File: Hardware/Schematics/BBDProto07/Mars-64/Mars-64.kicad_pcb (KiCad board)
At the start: 4 copper layers, 50.8 x 50.8 mm, 76 parts, among them J101 Conn_Coaxial, J102 Conn_Coaxial, U101 ADG731, U102 ADG731

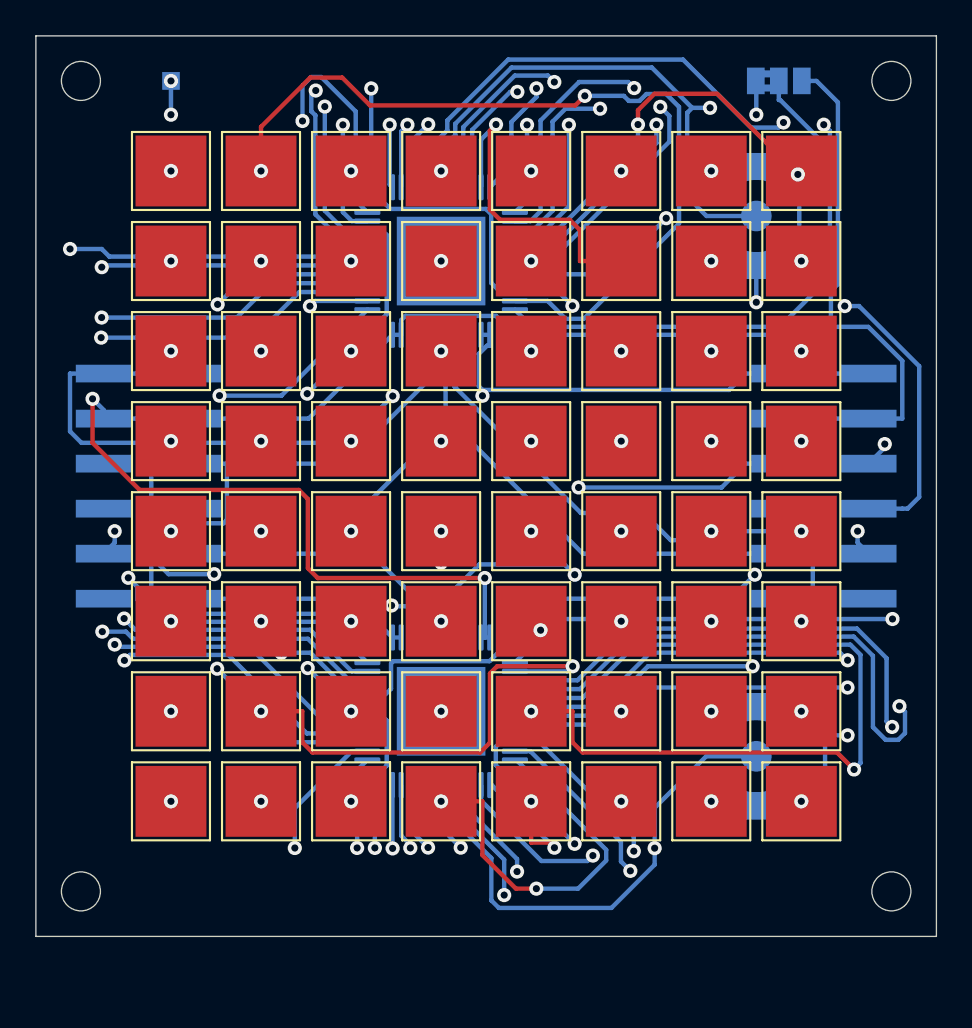
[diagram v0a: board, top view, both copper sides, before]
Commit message: Changed the position of the Pmod pads
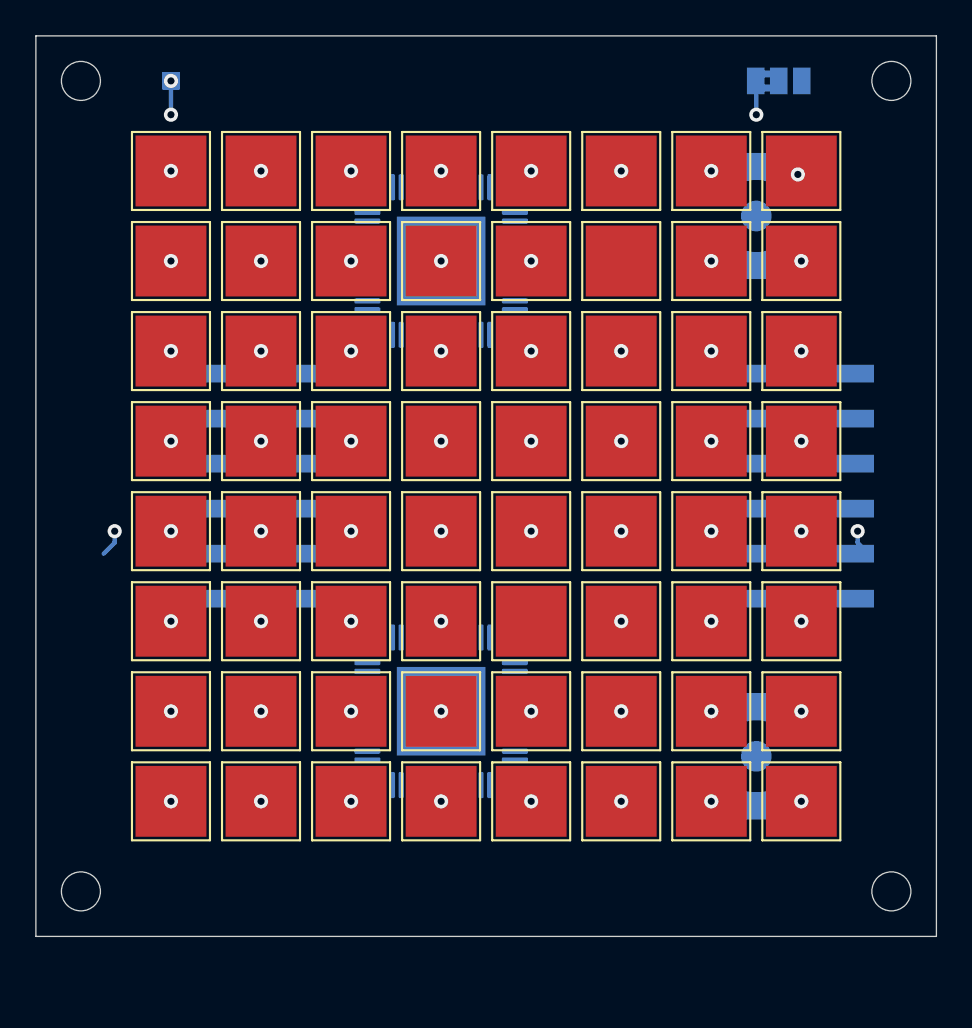
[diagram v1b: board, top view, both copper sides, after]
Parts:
- moved PmodF2 6.35 mm to (48.3, 55.9)
- moved PmodM1 1.27 mm to (78.7, 55.9)
- renumbered Pmod2 to PmodF2, Pmod1 to PmodM1
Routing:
- net GND: track 110.2 -> 0.00 mm, vias 2 -> 0
- net /VCC3V3: track 85.2 -> 0.00 mm, vias 2 -> 0
- net Net-(TP217-Pad1): track 83.9 -> 0.00 mm, vias 2 -> 1
- net Net-(TP208-Pad1): track 82.4 -> 0.00 mm, vias 2 -> 1
- net /SPI_CLK: track 78.6 -> 0.00 mm, vias 3 -> 0
- net Net-(TP123-Pad1): track 70.9 -> 0.00 mm, vias 2 -> 1
- net Net-(TP101-Pad1): track 69.0 -> 0.00 mm, vias 2 -> 1
- net /~SPI_CE: track 64.3 -> 0.00 mm, vias 2 -> 0
- net /DA: track 63.2 -> 0.00 mm, vias 2 -> 0
- net Net-(TP119-Pad1): track 62.1 -> 0.00 mm, vias 2 -> 1
- net /DB: track 61.7 -> 0.00 mm, vias 2 -> 0
- net Net-(TP122-Pad1): track 61.3 -> 0.00 mm, vias 2 -> 1
- net Net-(J101-Pad2): track 61.0 -> 0.00 mm, vias 2 -> 0
- net Net-(TP111-Pad1): track 60.2 -> 0.00 mm, vias 2 -> 1
- net Net-(TP120-Pad1): track 59.2 -> 0.00 mm, vias 2 -> 1
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
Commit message: Removed the EP from the footprint of the multiplexers
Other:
- board text added: "BBD Mars-64 rev. B"
- board text removed: "BBD Mars-64 rev. A"
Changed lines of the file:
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@@
     (title Mars-64)
     (date 2020-01-24)
-    (rev A)
+    (rev B)
     (company "Bio Balance Detector")
   )
@@
     (solder_mask_min_width 0.25)
     (aux_axis_origin 0 0)
-    (visible_elements 7FFFFFFF)
+    (visible_elements 7FFF7FFF)
     (pcbplotparams
       (layerselection 0x010fc_ffffffff)
@@
     )
   )
-  (gr_text "BBD Mars-64 rev. A" (at 60.96 78.74) (layer B.SilkS)
+  (gr_text "BBD Mars-64 rev. B" (at 60.96 78.74) (layer B.SilkS)
     (effects (font (size 1.5 1.5) (thickness 0.3)) (justify mirror))
   )

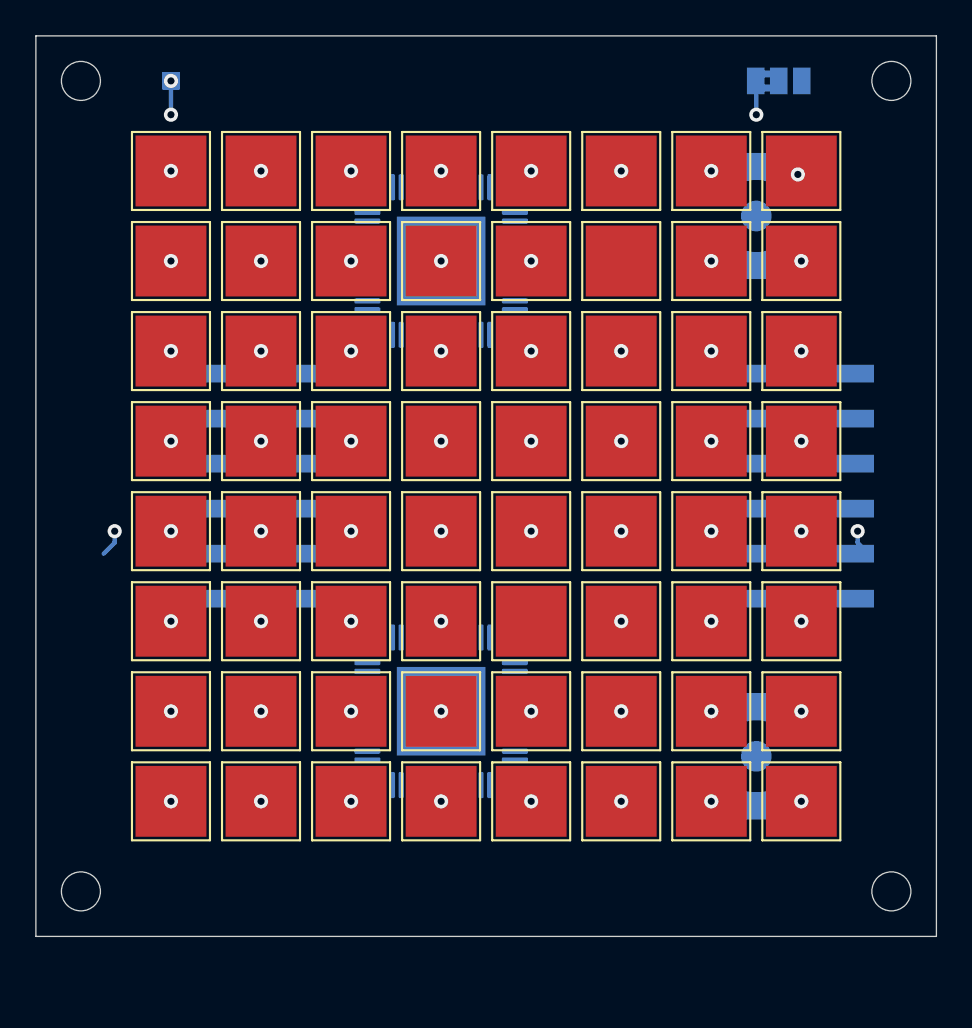
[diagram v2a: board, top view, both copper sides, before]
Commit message: Replaced the older footprints of U101 and U201
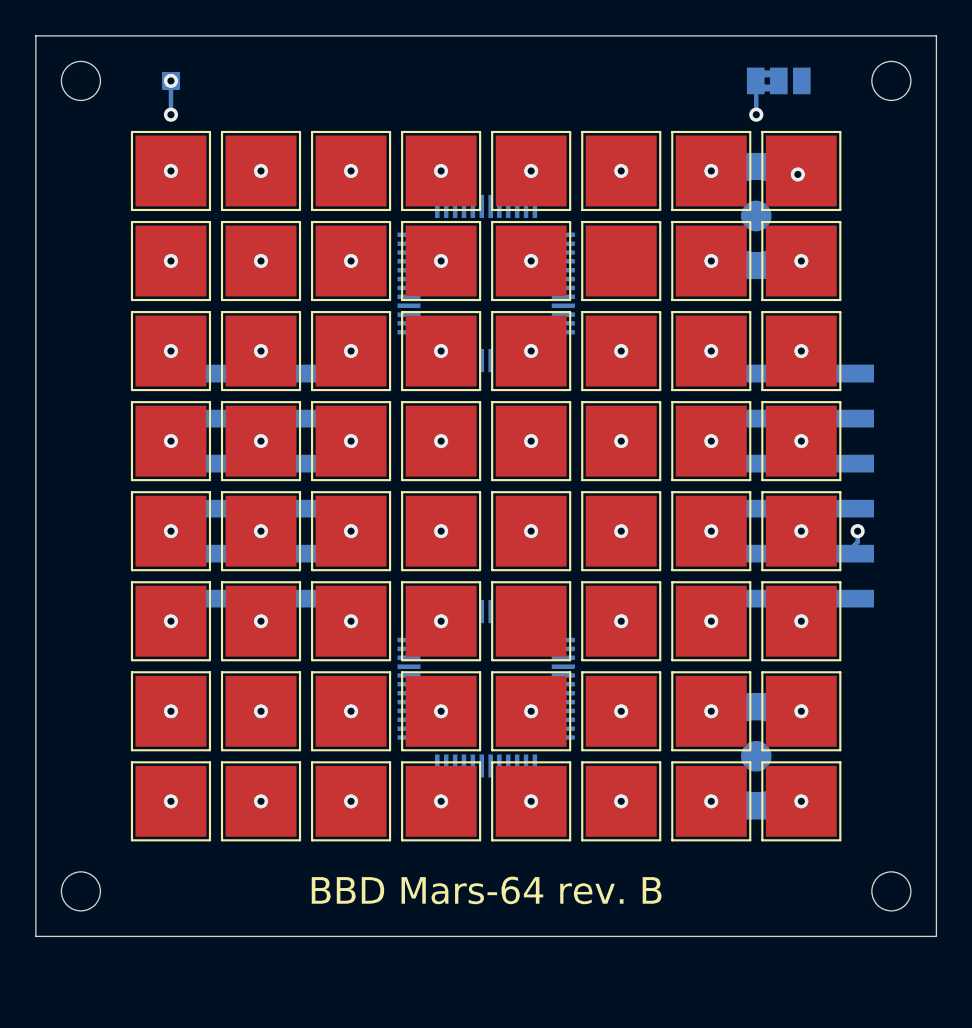
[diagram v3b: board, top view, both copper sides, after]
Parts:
- U101, U102: footprint Package_QFP:TQFP-48-1EP_7x7mm_P0.5mm_EP5x5mm -> Package_QFP:TQFP-48_7x7mm_P0.5mm
- moved U101 2.84 mm to (61.0, 44.5), turned to 0 degrees
- moved U102 2.84 mm to (61.0, 67.3)
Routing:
- net /AGND: track 57.5 -> 62.3 mm

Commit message: Rotated the U101
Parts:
- turned U101 to 180 degrees
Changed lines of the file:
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@@
   )
   (module Package_QFP:TQFP-48_7x7mm_P0.5mm (layer B.Cu)
-    (at 60.96 44.45)
+    (at 60.96 44.45 180)
     (descr "48 LEAD TQFP 7x7mm (see MICREL TQFP7x7-48LD-PL-1.pdf)")
     (tags "QFP 0.5")
@@
     (fp_line (start 3.625 3.625) (end 3.1 3.625) (layer B.SilkS) (width 0.15))
     (fp_line (start -3.625 3.2) (end -5 3.2) (layer B.SilkS) (width 0.15))
-    (pad 1 smd rect (at -4.35 2.75) (size 1.3 0.25) (layers B.Cu B.Paste B.Mask)
+    (pad 1 smd rect (at -4.35 2.75 180) (size 1.3 0.25) (layers B.Cu B.Paste B.Mask)
       (net 20 "Net-(TP112-Pad1)"))
-    (pad 2 smd rect (at -4.35 2.25) (size 1.3 0.25) (layers B.Cu B.Paste B.Mask)
+    (pad 2 smd rect (at -4.35 2.25 180) (size 1.3 0.25) (layers B.Cu B.Paste B.Mask)
       (net 19 "Net-(TP111-Pad1)"))
-    (pad 3 smd rect (at -4.35 1.75) (size 1.3 0.25) (layers B.Cu B.Paste B.Mask)
+    (pad 3 smd rect (at -4.35 1.75 180) (size 1.3 0.25) (layers B.Cu B.Paste B.Mask)
       (net 18 "Net-(TP110-Pad1)"))
-    (pad 4 smd rect (at -4.35 1.25) (size 1.3 0.25) (layers B.Cu B.Paste B.Mask)
+    (pad 4 smd rect (at -4.35 1.25 180) (size 1.3 0.25) (layers B.Cu B.Paste B.Mask)
       (net 17 "Net-(TP109-Pad1)"))
-    (pad 5 smd rect (at -4.35 0.75) (size 1.3 0.25) (layers B.Cu B.Paste B.Mask)
+    (pad 5 smd rect (at -4.35 0.75 180) (size 1.3 0.25) (layers B.Cu B.Paste B.Mask)
       (net 16 "Net-(TP108-Pad1)"))
-    (pad 6 smd rect (at -4.35 0.25) (size 1.3 0.25) (layers B.Cu B.Paste B.Mask)
+    (pad 6 smd rect (at -4.35 0.25 180) (size 1.3 0.25) (layers B.Cu B.Paste B.Mask)
       (net 15 "Net-(TP107-Pad1)"))
-    (pad 7 smd rect (at -4.35 -0.25) (size 1.3 0.25) (layers B.Cu B.Paste B.Mask)
+    (pad 7 smd rect (at -4.35 -0.25 180) (size 1.3 0.25) (layers B.Cu B.Paste B.Mask)
       (net 14 "Net-(TP106-Pad1)"))
-    (pad 8 smd rect (at -4.35 -0.75) (size 1.3 0.25) (layers B.Cu B.Paste B.Mask)
+    (pad 8 smd rect (at -4.35 -0.75 180) (size 1.3 0.25) (layers B.Cu B.Paste B.Mask)
       (net 13 "Net-(TP105-Pad1)"))
-    (pad 9 smd rect (at -4.35 -1.25) (size 1.3 0.25) (layers B.Cu B.Paste B.Mask)
+    (pad 9 smd rect (at -4.35 -1.25 180) (size 1.3 0.25) (layers B.Cu B.Paste B.Mask)
       (net 12 "Net-(TP104-Pad1)"))
-    (pad 10 smd rect (at -4.35 -1.75) (size 1.3 0.25) (layers B.Cu B.Paste B.Mask)
+    (pad 10 smd rect (at -4.35 -1.75 180) (size 1.3 0.25) (layers B.Cu B.Paste B.Mask)
       (net 11 "Net-(TP103-Pad1)"))
-    (pad 11 smd rect (at -4.35 -2.25) (size 1.3 0.25) (layers B.Cu B.Paste B.Mask)
+    (pad 11 smd rect (at -4.35 -2.25 180) (size 1.3 0.25) (layers B.Cu B.Paste B.Mask)
       (net 10 "Net-(TP102-Pad1)"))
-    (pad 12 smd rect (at -4.35 -2.75) (size 1.3 0.25) (layers B.Cu B.Paste B.Mask)
+    (pad 12 smd rect (at -4.35 -2.75 180) (size 1.3 0.25) (layers B.Cu B.Paste B.Mask)
       (net 9 "Net-(TP101-Pad1)"))
-    (pad 13 smd rect (at -2.75 -4.35 270) (size 1.3 0.25) (layers B.Cu B.Paste B.Mask)
+    (pad 13 smd rect (at -2.75 -4.35 90) (size 1.3 0.25) (layers B.Cu B.Paste B.Mask)
       (net 5 /VCC3V3))
-    (pad 14 smd rect (at -2.25 -4.35 270) (size 1.3 0.25) (layers B.Cu B.Paste B.Mask)
+    (pad 14 smd rect (at -2.25 -4.35 90) (size 1.3 0.25) (layers B.Cu B.Paste B.Mask)
       (net 5 /VCC3V3))
-    (pad 15 smd rect (at -1.75 -4.35 270) (size 1.3 0.25) (layers B.Cu B.Paste B.Mask))
-    (pad 16 smd rect (at -1.25 -4.35 270) (size 1.3 0.25) (layers B.Cu B.Paste B.Mask))
-    (pad 17 smd rect (at -0.75 -4.35 270) (size 1.3 0.25) (layers B.Cu B.Paste B.Mask)
+    (pad 15 smd rect (at -1.75 -4.35 90) (size 1.3 0.25) (layers B.Cu B.Paste B.Mask))
+    (pad 16 smd rect (at -1.25 -4.35 90) (size 1.3 0.25) (layers B.Cu B.Paste B.Mask))
+    (pad 17 smd rect (at -0.75 -4.35 90) (size 1.3 0.25) (layers B.Cu B.Paste B.Mask)
       (net 1 /~SPI_CE))
-    (pad 18 smd rect (at -0.25 -4.35 270) (size 1.3 0.25) (layers B.Cu B.Paste B.Mask)
+    (pad 18 smd rect (at -0.25 -4.35 90) (size 1.3 0.25) (layers B.Cu B.Paste B.Mask)
       (net 2 /SPI_MOSI))
-    (pad 19 smd rect (at 0.25 -4.35 270) (size 1.3 0.25) (layers B.Cu B.Paste B.Mask)
+    (pad 19 smd rect (at 0.25 -4.35 90) (size 1.3 0.25) (layers B.Cu B.Paste B.Mask)
       (net 3 /SPI_CLK))
-    (pad 20 smd rect (at 0.75 -4.35 270) (size 1.3 0.25) (layers B.Cu B.Paste B.Mask))
-    (pad 21 smd rect (at 1.25 -4.35 270) (size 1.3 0.25) (layers B.Cu B.Paste B.Mask))
-    (pad 22 smd rect (at 1.75 -4.35 270) (size 1.3 0.25) (layers B.Cu B.Paste B.Mask))
-    (pad 23 smd rect (at 2.25 -4.35 270) (size 1.3 0.25) (layers B.Cu B.Paste B.Mask)
+    (pad 20 smd rect (at 0.75 -4.35 90) (size 1.3 0.25) (layers B.Cu B.Paste B.Mask))
+    (pad 21 smd rect (at 1.25 -4.35 90) (size 1.3 0.25) (layers B.Cu B.Paste B.Mask))
+    (pad 22 smd rect (at 1.75 -4.35 90) (size 1.3 0.25) (layers B.Cu B.Paste B.Mask))
+    (pad 23 smd rect (at 2.25 -4.35 90) (size 1.3 0.25) (layers B.Cu B.Paste B.Mask)
       (net 4 GND))
-    (pad 24 smd rect (at 2.75 -4.35 270) (size 1.3 0.25) (layers B.Cu B.Paste B.Mask)
+    (pad 24 smd rect (at 2.75 -4.35 90) (size 1.3 0.25) (layers B.Cu B.Paste B.Mask)
       (net 4 GND))
-    (pad 25 smd rect (at 4.35 -2.75) (size 1.3 0.25) (layers B.Cu B.Paste B.Mask)
+    (pad 25 smd rect (at 4.35 -2.75 180) (size 1.3 0.25) (layers B.Cu B.Paste B.Mask)
       (net 25 "Net-(TP117-Pad1)"))
-    (pad 26 smd rect (at 4.35 -2.25) (size 1.3 0.25) (layers B.Cu B.Paste B.Mask)
+    (pad 26 smd rect (at 4.35 -2.25 180) (size 1.3 0.25) (layers B.Cu B.Paste B.Mask)
       (net 26 "Net-(TP118-Pad1)"))
-    (pad 27 smd rect (at 4.35 -1.75) (size 1.3 0.25) (layers B.Cu B.Paste B.Mask)
+    (pad 27 smd rect (at 4.35 -1.75 180) (size 1.3 0.25) (layers B.Cu B.Paste B.Mask)
       (net 27 "Net-(TP119-Pad1)"))
-    (pad 28 smd rect (at 4.35 -1.25) (size 1.3 0.25) (layers B.Cu B.Paste B.Mask)
+    (pad 28 smd rect (at 4.35 -1.25 180) (size 1.3 0.25) (layers B.Cu B.Paste B.Mask)
       (net 28 "Net-(TP120-Pad1)"))
-    (pad 29 smd rect (at 4.35 -0.75) (size 1.3 0.25) (layers B.Cu B.Paste B.Mask)
+    (pad 29 smd rect (at 4.35 -0.75 180) (size 1.3 0.25) (layers B.Cu B.Paste B.Mask)
       (net 29 "Net-(TP121-Pad1)"))
-    (pad 30 smd rect (at 4.35 -0.25) (size 1.3 0.25) (layers B.Cu B.Paste B.Mask)
+    (pad 30 smd rect (at 4.35 -0.25 180) (size 1.3 0.25) (layers B.Cu B.Paste B.Mask)
       (net 30 "Net-(TP122-Pad1)"))
-    (pad 31 smd rect (at 4.35 0.25) (size 1.3 0.25) (layers B.Cu B.Paste B.Mask)
+    (pad 31 smd rect (at 4.35 0.25 180) (size 1.3 0.25) (layers B.Cu B.Paste B.Mask)
       (net 31 "Net-(TP123-Pad1)"))
-    (pad 32 smd rect (at 4.35 0.75) (size 1.3 0.25) (layers B.Cu B.Paste B.Mask)
+    (pad 32 smd rect (at 4.35 0.75 180) (size 1.3 0.25) (layers B.Cu B.Paste B.Mask)
       (net 32 "Net-(TP124-Pad1)"))
-    (pad 33 smd rect (at 4.35 1.25) (size 1.3 0.25) (layers B.Cu B.Paste B.Mask)
+    (pad 33 smd rect (at 4.35 1.25 180) (size 1.3 0.25) (layers B.Cu B.Paste B.Mask)
       (net 33 "Net-(TP125-Pad1)"))
-    (pad 34 smd rect (at 4.35 1.75) (size 1.3 0.25) (layers B.Cu B.Paste B.Mask)
+    (pad 34 smd rect (at 4.35 1.75 180) (size 1.3 0.25) (layers B.Cu B.Paste B.Mask)
       (net 34 "Net-(TP126-Pad1)"))
-    (pad 35 smd rect (at 4.35 2.25) (size 1.3 0.25) (layers B.Cu B.Paste B.Mask)
+    (pad 35 smd rect (at 4.35 2.25 180) (size 1.3 0.25) (layers B.Cu B.Paste B.Mask)
       (net 35 "Net-(TP127-Pad1)"))
-    (pad 36 smd rect (at 4.35 2.75) (size 1.3 0.25) (layers B.Cu B.Paste B.Mask)
+    (pad 36 smd rect (at 4.35 2.75 180) (size 1.3 0.25) (layers B.Cu B.Paste B.Mask)
       (net 36 "Net-(TP128-Pad1)"))
-    (pad 37 smd rect (at 2.75 4.35 270) (size 1.3 0.25) (layers B.Cu B.Paste B.Mask)
+    (pad 37 smd rect (at 2.75 4.35 90) (size 1.3 0.25) (layers B.Cu B.Paste B.Mask)
       (net 37 "Net-(TP129-Pad1)"))
-    (pad 38 smd rect (at 2.25 4.35 270) (size 1.3 0.25) (layers B.Cu B.Paste B.Mask)
+    (pad 38 smd rect (at 2.25 4.35 90) (size 1.3 0.25) (layers B.Cu B.Paste B.Mask)
       (net 38 "Net-(TP130-Pad1)"))
-    (pad 39 smd rect (at 1.75 4.35 270) (size 1.3 0.25) (layers B.Cu B.Paste B.Mask)
+    (pad 39 smd rect (at 1.75 4.35 90) (size 1.3 0.25) (layers B.Cu B.Paste B.Mask)
       (net 39 "Net-(TP131-Pad1)"))
-    (pad 40 smd rect (at 1.25 4.35 270) (size 1.3 0.25) (layers B.Cu B.Paste B.Mask)
+    (pad 40 smd rect (at 1.25 4.35 90) (size 1.3 0.25) (layers B.Cu B.Paste B.Mask)
       (net 40 "Net-(TP132-Pad1)"))
-    (pad 41 smd rect (at 0.75 4.35 270) (size 1.3 0.25) (layers B.Cu B.Paste B.Mask))
-    (pad 42 smd rect (at 0.25 4.35 270) (size 1.3 0.25) (layers B.Cu B.Paste B.Mask))
-    (pad 43 smd rect (at -0.25 4.35 270) (size 1.3 0.25) (layers B.Cu B.Paste B.Mask)
+    (pad 41 smd rect (at 0.75 4.35 90) (size 1.3 0.25) (layers B.Cu B.Paste B.Mask))
+    (pad 42 smd rect (at 0.25 4.35 90) (size 1.3 0.25) (layers B.Cu B.Paste B.Mask))
+    (pad 43 smd rect (at -0.25 4.35 90) (size 1.3 0.25) (layers B.Cu B.Paste B.Mask)
       (net 7 /DA))
-    (pad 44 smd rect (at -0.75 4.35 270) (size 1.3 0.25) (layers B.Cu B.Paste B.Mask))
-    (pad 45 smd rect (at -1.25 4.35 270) (size 1.3 0.25) (layers B.Cu B.Paste B.Mask)
+    (pad 44 smd rect (at -0.75 4.35 90) (size 1.3 0.25) (layers B.Cu B.Paste B.Mask))
+    (pad 45 smd rect (at -1.25 4.35 90) (size 1.3 0.25) (layers B.Cu B.Paste B.Mask)
       (net 24 "Net-(TP116-Pad1)"))
-    (pad 46 smd rect (at -1.75 4.35 270) (size 1.3 0.25) (layers B.Cu B.Paste B.Mask)
+    (pad 46 smd rect (at -1.75 4.35 90) (size 1.3 0.25) (layers B.Cu B.Paste B.Mask)
       (net 23 "Net-(TP115-Pad1)"))
-    (pad 47 smd rect (at -2.25 4.35 270) (size 1.3 0.25) (layers B.Cu B.Paste B.Mask)
+    (pad 47 smd rect (at -2.25 4.35 90) (size 1.3 0.25) (layers B.Cu B.Paste B.Mask)
       (net 22 "Net-(TP114-Pad1)"))
-    (pad 48 smd rect (at -2.75 4.35 270) (size 1.3 0.25) (layers B.Cu B.Paste B.Mask)
+    (pad 48 smd rect (at -2.75 4.35 90) (size 1.3 0.25) (layers B.Cu B.Paste B.Mask)
       (net 21 "Net-(TP113-Pad1)"))
     (model ${KISYS3DMOD}/Package_QFP.3dshapes/TQFP-48_7x7mm_P0.5mm.wrl

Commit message: Completed the routing of Mars-64 rev B
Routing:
- net GND: track 0.00 -> 89.8 mm, vias 0 -> 2
- net /SPI_MOSI: track 0.00 -> 83.4 mm, vias 0 -> 2
- net Net-(TP101-Pad1): track 0.00 -> 72.4 mm, vias 1 -> 2
- net /DA: track 0.00 -> 70.5 mm
- net Net-(TP123-Pad1): track 0.00 -> 69.1 mm, vias 1 -> 2
- net Net-(TP219-Pad1): track 0.00 -> 66.1 mm, vias 1 -> 2
- net Net-(TP122-Pad1): track 0.00 -> 65.0 mm, vias 1 -> 2
- net /~SPI_CE: track 0.00 -> 64.2 mm, vias 0 -> 2
- net Net-(J101-Pad2): track 0.00 -> 64.1 mm, vias 0 -> 3
- net Net-(TP217-Pad1): track 0.00 -> 60.4 mm, vias 1 -> 2
- net Net-(TP120-Pad1): track 0.00 -> 59.8 mm, vias 1 -> 2
- net /VCC3V3: track 0.00 -> 58.3 mm
- net Net-(TP104-Pad1): track 0.00 -> 58.1 mm, vias 1 -> 2
- net Net-(TP124-Pad1): track 0.00 -> 57.0 mm, vias 1 -> 2
- net Net-(TP121-Pad1): track 0.00 -> 53.5 mm, vias 1 -> 2
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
